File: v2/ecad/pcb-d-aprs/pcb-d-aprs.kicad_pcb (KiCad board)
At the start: 4 copper layers, 80 x 62 mm, 95 parts, among them Q1 BC847 (PTT2, spare), Q2 BC847 (PTT to the module), Q3 2N7002 (EMCON inhibit in Q2 e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, Q4 BC857 (TR mirror from RADIO_P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, U1 TPS61089 boost 7.6 V / 2 A, U2 DNP bench: DMR858M 5 W UHF mo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, U5 WM8960 audio codec QFN-32 (pi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, U7 PCA9555PW 0x26: PTT, PTT2, LE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, U8 SC16IS740IPW I2C-to-UART brid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, X1 24 MHz 3.3 V oscillator 3225 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

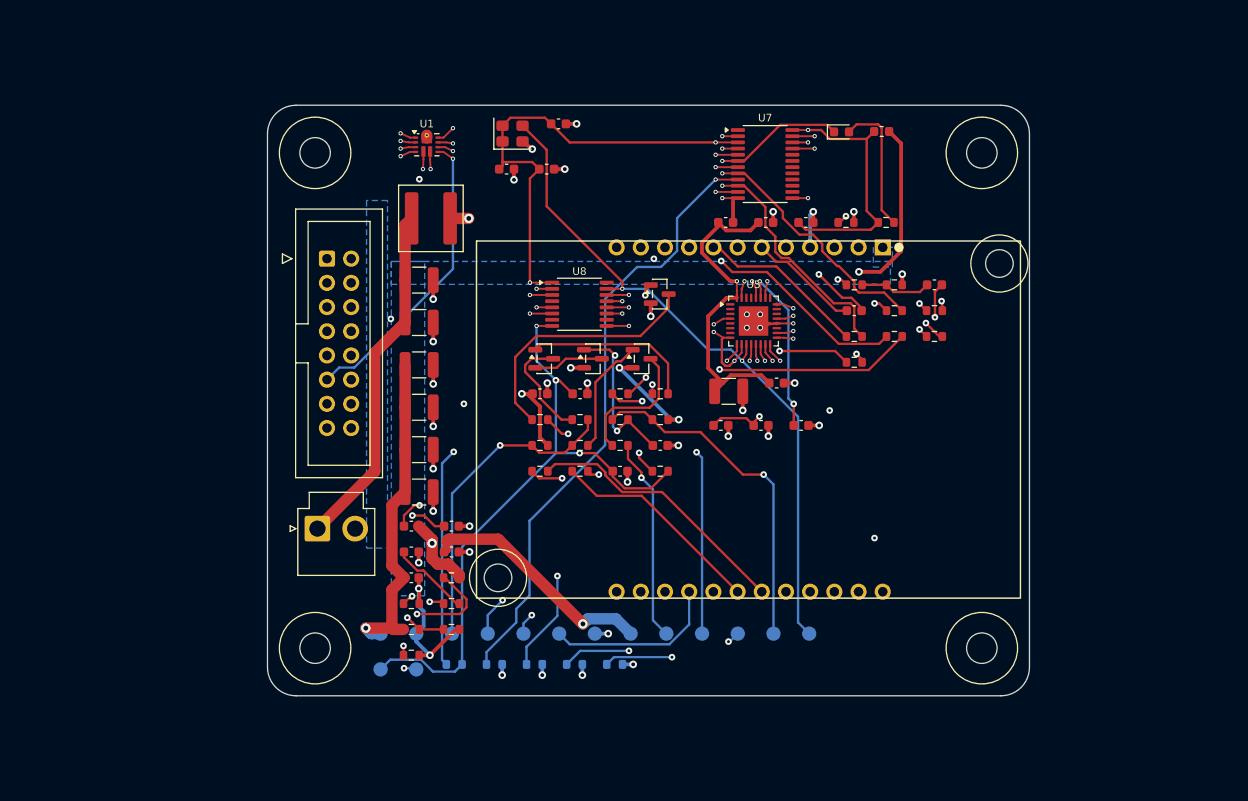
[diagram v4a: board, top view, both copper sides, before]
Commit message: feat(pcb-d): D7 routed and finished for the DMR858M V1.0 board [MESHSAT-804]
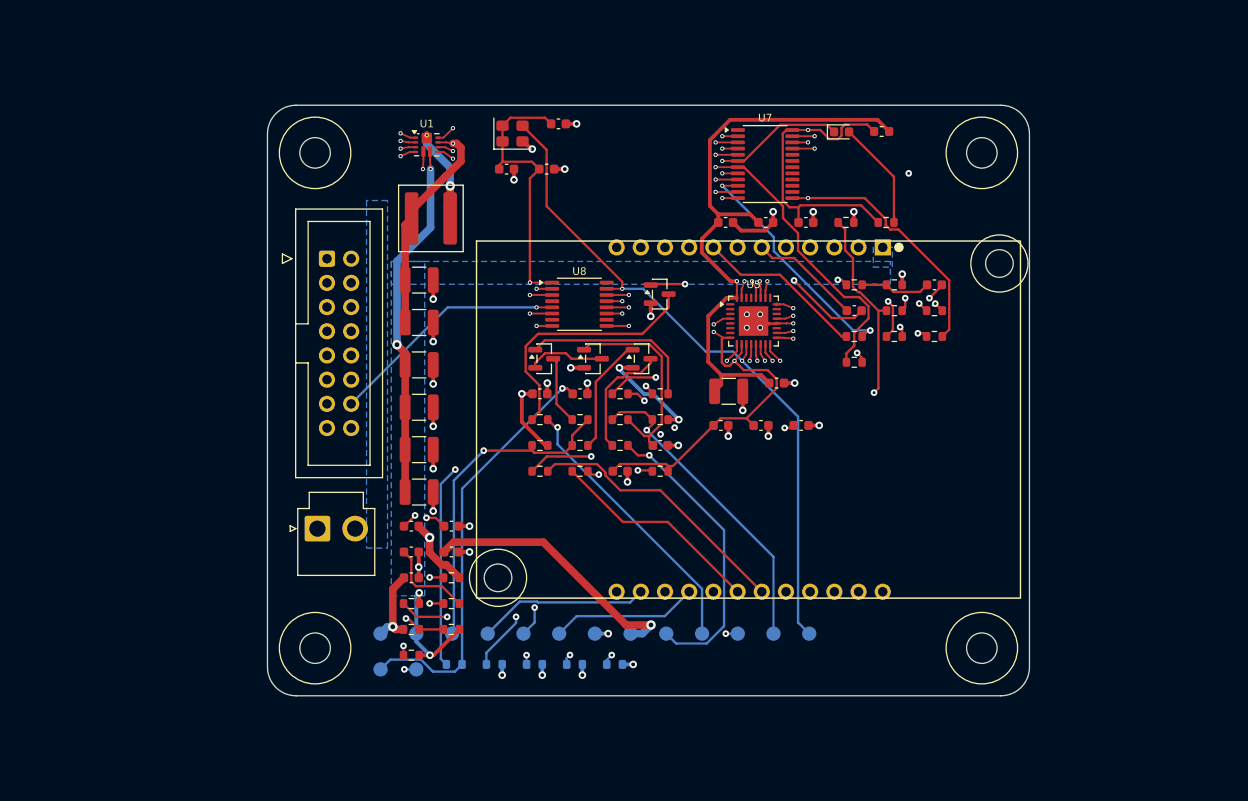
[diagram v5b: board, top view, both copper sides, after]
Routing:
- net /V8: track 36.9 -> 126.7 mm, vias 2 -> 3
- net GND: track 382.2 -> 454.6 mm
- net /VIN_CELL: track 95.6 -> 147.3 mm
- net /MEZZ_EN: track 99.3 -> 131.8 mm
- net /CH2_IN: track 84.9 -> 106.6 mm
- net /RADIO_SPK: track 80.2 -> 63.2 mm
- net /TX_INHIBIT_n: track 83.9 -> 69.1 mm
- net /SW: track 69.5 -> 55.3 mm
- net /RADIO_COS: track 77.9 -> 65.2 mm, vias 3 -> 1
- net /FSW: track 63.6 -> 51.3 mm
- net /+3V3_AB: track 230.1 -> 241.5 mm, vias 12 -> 10
- net /TR_APRS: track 67.6 -> 77.7 mm
- net /SDA: track 82.1 -> 92.1 mm, vias 4 -> 3
- net /RADIO_PTT: track 91.3 -> 81.4 mm, vias 1 -> 2
- net /RADIO_COS_IN: track 26.1 -> 35.9 mm, vias 1 -> 3
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
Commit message: fix(pcb): A21 and D7 boards retitled to their phase and date, deliverables re-exported [MESHSAT-795]
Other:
- board text added: "PCB-D APRS BOARD REV A (D7) | MESHSAT-709/748/804 | 2026-09-05"
- board text removed: "PCB-D APRS BOARD REV A (D5) | MESHSAT-709/748 | 2026-09-03"
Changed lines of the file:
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@@
 	(title_block
 		(title "MeshSat Field Kit carrier - PCB-D APRS BOARD")
-		(date "2026-09-02")
-		(rev "A")
+		(date "2026-09-05")
+		(rev "A (D7)")
 		(company "MeshSat")
 		(comment 1 "MESHSAT-709 / MESHSAT-748. Board-local frame, +X = case east. Phase D1 mechanical + placement. tools/gen_pcb_d.py")
@@
 		)
 	)
-	(gr_text "PCB-D APRS BOARD REV A (D5) | MESHSAT-709/748 | 2026-09-03"
+	(gr_text "PCB-D APRS BOARD REV A (D7) | MESHSAT-709/748/804 | 2026-09-05"
 		(at 110 101.5 0)
 		(layer "B.SilkS")

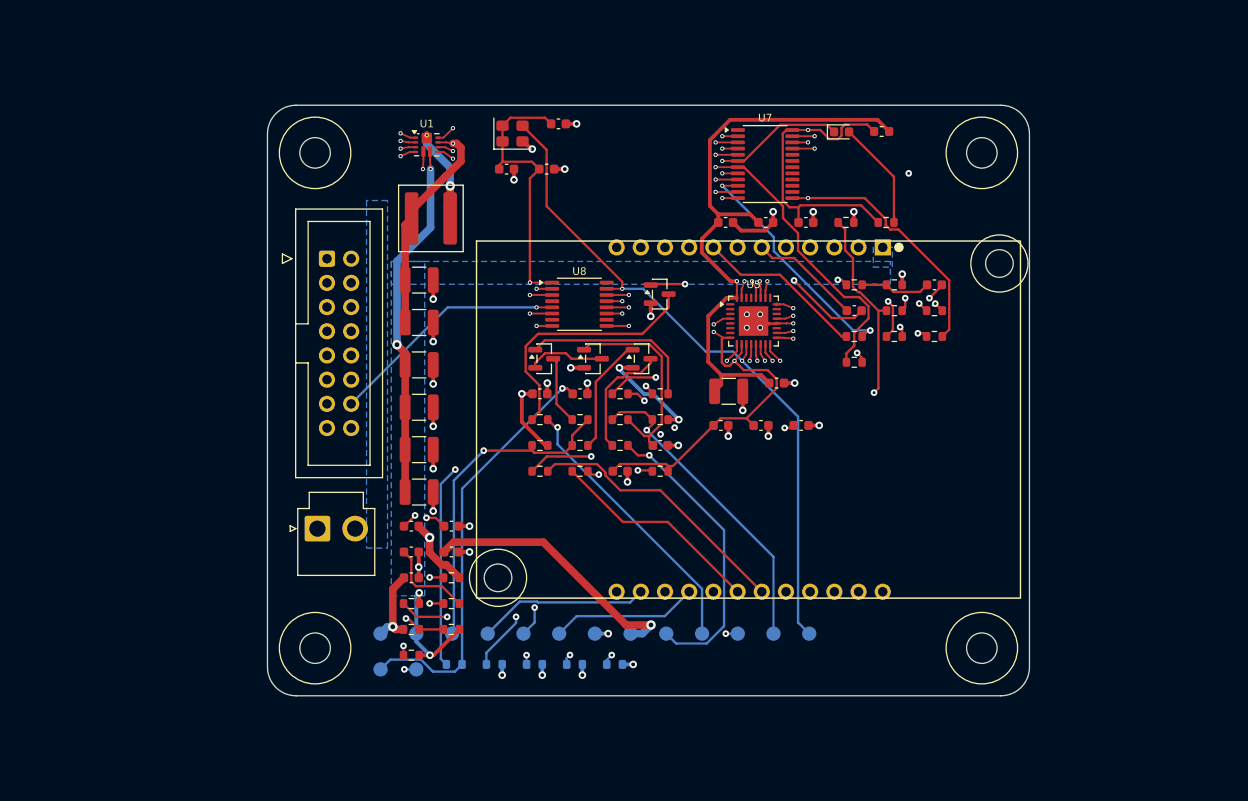
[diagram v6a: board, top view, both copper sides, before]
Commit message: feat(ecad): D8 routed clean and released (SA868 exciter, T/R relay, LPF, USB audio and control set), C7 generators (backer ring, RP2040 panel controller, PDi e-paper driver, Xenarc face, headset jacks), per-closure stub acceptance, plane-net fanout fixes [MESHSAT-830]
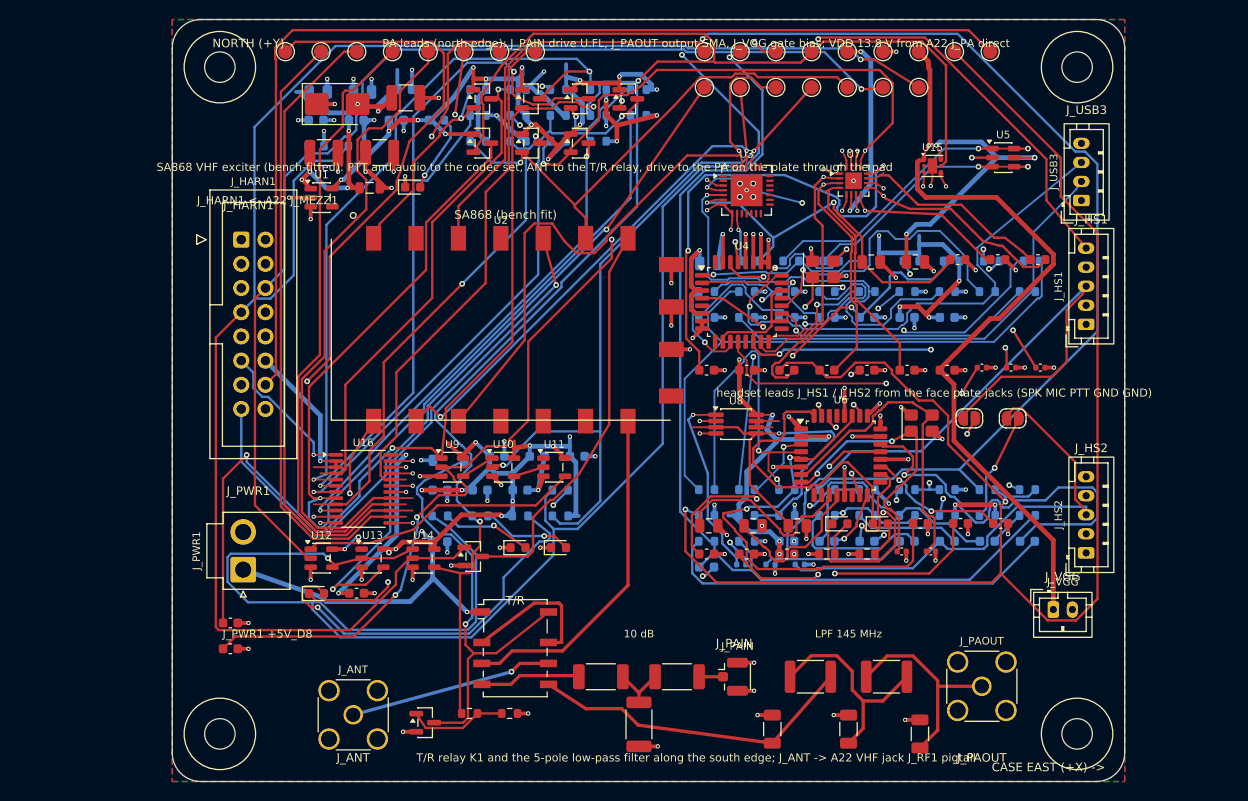
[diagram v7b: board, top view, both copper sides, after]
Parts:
- removed X1: 24 MHz 3.3 V oscillator 3225 (ASE-24.000MHZ-LC-T class), Oscillator_SMD_Abracon_ASE-4Pin_3.2x2.5mm
- added C1: 47u 6.3V X5R 1210, C_1210_3225Metric, F.Cu at (74.5, 68.2)
- added C11: 100n, C_0603_1608Metric, F.Cu at (132.5, 85.2)
- added C12: 1u, C_0603_1608Metric, B.Cu at (122.9, 91.3)
- added C15: 100n, C_0603_1608Metric, B.Cu at (127.2, 91.3)
- added C16: 100n, C_0603_1608Metric, B.Cu at (131.4, 91.3)
- added C19: 1u, C_0603_1608Metric, F.Cu at (128.6, 112.9)
- added C2: 47u 6.3V X5R 1210, C_1210_3225Metric, F.Cu at (65.9, 74.0)
- added C3: 10u, C_0805_2012Metric, B.Cu at (65.3, 67.6)
- added C31: 1u, C_0603_1608Metric, F.Cu at (106.1, 96.8)
- added C4: 100n, C_0603_1608Metric, B.Cu at (74.4, 67.4)
- added C41: 1u, C_0603_1608Metric, B.Cu at (127.2, 114.8)
- added C42: 1u, C_0603_1608Metric, B.Cu at (131.4, 114.8)
- added C43: 100p NP0, C_0402_1005Metric, B.Cu at (109.7, 117.2)
- added C44: 1n NP0, C_0402_1005Metric, B.Cu at (112.8, 117.2)
- added C45: 1n NP0, C_0402_1005Metric, B.Cu at (115.9, 117.2)
- added C46: 1u, C_0603_1608Metric, B.Cu at (135.6, 114.8)
- added C47: 1u, C_0603_1608Metric, B.Cu at (139.8, 114.8)
- added C48: 1u, C_0603_1608Metric, B.Cu at (106.1, 117.5)
- added C49: 100n, C_0603_1608Metric, F.Cu at (56.1, 123.4)
- added C5: 47u 6.3V X5R 1210, C_1210_3225Metric, F.Cu at (71.8, 74.0)
- added C50: 100n, C_0603_1608Metric, F.Cu at (56.1, 126.1)
- added C51: 100n, C_0603_1608Metric, B.Cu at (84.1, 105.9)
- added C52: 100n, C_0603_1608Metric, B.Cu at (88.3, 105.9)
- added C53: 100n, C_0603_1608Metric, B.Cu at (92.5, 105.9)
- added C54: 100n, C_0603_1608Metric, B.Cu at (78.1, 109.4)
- added C55: 100n, C_0603_1608Metric, B.Cu at (82.3, 109.4)
- added C56: 100n, C_0603_1608Metric, B.Cu at (86.5, 109.4)
- added C57: 100n, C_0603_1608Metric, B.Cu at (78.1, 114.8)
- added C58: 22p 500V NP0 1206, C_1206_3216Metric, F.Cu at (128.5, 135.0)
- added C59: 39p 500V NP0 1206, C_1206_3216Metric, F.Cu at (121.0, 134.5)
- added C6: 100n, C_0603_1608Metric, B.Cu at (65.1, 70.6)
- added C60: 22p 500V NP0 1206, C_1206_3216Metric, F.Cu at (113.0, 134.5)
- added C61: 4.7n, C_0402_1005Metric, F.Cu at (141.1, 96.5)
- added C62: 100n, C_0603_1608Metric, F.Cu at (131.4, 96.8)
- added C63: 100n, C_0603_1608Metric, F.Cu at (69.4, 120.2)
- added D2: 1N4148W coil flyback, D_SOD-123, B.Cu at (79.0, 106.3)
- added JP1: electret bias headset 1 (close for an electret microphone), SolderJumper-2_P1.3mm_Open_RoundedPad1.0x1.5mm, F.Cu at (133.7, 101.9)
- added JP2: electret bias headset 2, SolderJumper-2_P1.3mm_Open_RoundedPad1.0x1.5mm, F.Cu at (138.2, 101.9)
- added J_ANT: antenna (SMA, pigtail to A22's VHF jack J_RF1), SMA_Amphenol_132134_Vertical, F.Cu at (69.0, 133.0)
- added J_HS1: headset 1 lead (JST-PH 1x5 to the face plate U-174/U jack):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, JST_PH_B5B-PH-K_1x05_P2.00mm_Vertical, F.Cu at (145.9, 92.0)
- added J_HS2: headset 2 lead (JST-PH 1x5 to the face plate U-174/U jack):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, JST_PH_B5B-PH-K_1x05_P2.00mm_Vertical, F.Cu at (145.9, 116.0)
- added J_PAIN: PA drive (U.FL, coax to the RA30H1317M1 input on the plate), U.FL_Hirose_U.FL-R-SMT-1_Vertical, F.Cu at (108.9, 129.0)
- added J_PAOUT: PA output (SMA, coax from the RA30H1317M1 output on the pla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, SMA_Amphenol_132134_Vertical, F.Cu at (135.0, 130.0)
- added J_USB3: spare hub port 3 (JST-PH 1x4): 5V D- D+ GND, JST_PH_B4B-PH-K_1x04_P2.00mm_Vertical, F.Cu at (145.4, 79.0)
- added J_VGG: PA gate bias lead (JST-PH 1x2 to the RA30H1317M1 VGG): VGG 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, JST_PH_B2B-PH-K_1x02_P2.00mm_Vertical, F.Cu at (142.5, 122.0)
- added K1: Omron G6K-2F-Y 5 VDC DPDT signal relay, T/R, Relay_DPDT_Omron_G6K-2F-Y, F.Cu at (86.0, 126.0)
- added L2: 68nH 1812 (LPF), L_1812_4532Metric, F.Cu at (117.0, 129.0)
- added LED1: green power, LED_0603_1608Metric, F.Cu at (75.2, 77.6)
- added LED2: amber record, LED_0603_1608Metric, F.Cu at (120.1, 112.9)
- added LED3: green playback, LED_0603_1608Metric, F.Cu at (124.3, 112.9)
- added LED4: red transmit, LED_0603_1608Metric, F.Cu at (86.3, 115.4)
- added LED5: amber PA keyed, LED_0603_1608Metric, F.Cu at (90.6, 115.4)
- added LED6: green receive (AUDIO_ON low), LED_0603_1608Metric, F.Cu at (65.1, 120.3)
- added Q5: 2N7002, SOT-23, F.Cu at (92.8, 68.3)
- added Q6: 2N7002, SOT-23, F.Cu at (97.9, 68.3)
- added Q7: 2N7002, SOT-23, F.Cu at (82.6, 73.0)
- added Q8: 2N7002, SOT-23, F.Cu at (87.7, 73.0)
- added Q9: 2N7002, SOT-23, F.Cu at (92.8, 73.0)
- added R1: 2.2k, R_0603_1608Metric, B.Cu at (77.7, 70.6)
- added R14: 15k, R_0603_1608Metric, B.Cu at (110.3, 88.6)
- added R16: 22, R_0603_1608Metric, B.Cu at (118.7, 88.6)
- added R17: 22, R_0603_1608Metric, B.Cu at (122.9, 88.6)
- added R18: 15k, R_0603_1608Metric, B.Cu at (127.2, 88.6)
- added R19: 15k, R_0603_1608Metric, B.Cu at (131.4, 88.6)
- added R20: 22, R_0603_1608Metric, B.Cu at (135.6, 88.6)
- added R21: 22, R_0603_1608Metric, B.Cu at (139.8, 88.6)
- added R22: 15k, R_0603_1608Metric, B.Cu at (106.1, 91.3)
- added R23: 15k, R_0603_1608Metric, B.Cu at (110.3, 91.3)
- added R24: 15k, R_0603_1608Metric, B.Cu at (114.5, 91.3)
- added R25: 15k, R_0603_1608Metric, B.Cu at (118.7, 91.3)
- added R26: 33, R_0603_1608Metric, B.Cu at (106.1, 109.4)
- added R27: 33, R_0603_1608Metric, B.Cu at (110.3, 109.4)
- added R28: 1.5k, R_0603_1608Metric, B.Cu at (114.5, 109.4)
- added R29: 1k, R_0603_1608Metric, F.Cu at (118.7, 116.1)
- added R5: 10k, R_0603_1608Metric, B.Cu at (90.7, 112.1)
- added R53: 100k, R_0603_1608Metric, F.Cu at (85.4, 132.9)
- added R54: 27 1% 2010, R_2010_5025Metric, F.Cu at (95.0, 129.0)
- added R55: 36 1% 2010, R_2010_5025Metric, F.Cu at (99.0, 134.0)
- added R56: 27 1% 2010, R_2010_5025Metric, F.Cu at (103.0, 129.0)
- added R6: 22, R_0603_1608Metric, B.Cu at (115.0, 85.4)
- added R66: 10k, R_0603_1608Metric, B.Cu at (82.1, 67.4)
- added R67: 10k, R_0603_1608Metric, B.Cu at (86.3, 67.4)
- added R68: 10k, R_0603_1608Metric, B.Cu at (90.5, 67.4)
- added R69: 10k, R_0603_1608Metric, B.Cu at (94.7, 67.4)
- added R7: 22, R_0603_1608Metric, B.Cu at (119.2, 85.4)
- added R70: 10k, R_0603_1608Metric, B.Cu at (98.9, 67.4)
- added R71: 10k, R_0603_1608Metric, B.Cu at (82.1, 70.1)
- added R72: 10k, R_0603_1608Metric, B.Cu at (86.3, 70.1)
- added R73: 10k, R_0603_1608Metric, B.Cu at (90.5, 70.1)
- added R74: 10k, R_0603_1608Metric, B.Cu at (94.7, 70.1)
- added R75: 10k, R_0603_1608Metric, B.Cu at (98.9, 70.1)
- added R76: 10k, R_0603_1608Metric, B.Cu at (82.1, 72.8)
- added R77: 10k, R_0603_1608Metric, B.Cu at (86.3, 72.8)
- added R78: 10k, R_0603_1608Metric, B.Cu at (90.5, 72.8)
- added R79: 10k, R_0603_1608Metric, B.Cu at (94.7, 72.8)
- added TP16: PA_EN, TestPoint_Pad_D1.5mm, F.Cu at (128.4, 67.1)
- added TP17: EXP_SPARE1, TestPoint_Pad_D1.5mm, F.Cu at (61.9, 63.4)
- added TP18: EXP_SPARE2, TestPoint_Pad_D1.5mm, F.Cu at (65.6, 63.4)
- added TP19: EXP_SPARE3, TestPoint_Pad_D1.5mm, F.Cu at (69.4, 63.4)
- added TP20: EXP_SPARE4, TestPoint_Pad_D1.5mm, F.Cu at (73.1, 63.4)
- added TP21: EXP_SPARE5, TestPoint_Pad_D1.5mm, F.Cu at (76.9, 63.4)
- added TP22: EXP_SPARE6, TestPoint_Pad_D1.5mm, F.Cu at (80.6, 63.4)
- added TP23: EXP_SPARE7, TestPoint_Pad_D1.5mm, F.Cu at (84.4, 63.4)
- added TP24: EXP_SPARE8, TestPoint_Pad_D1.5mm, F.Cu at (88.1, 63.4)
- added U10: 74LVC1G08 AND: headsets AND software PTT (RTS), SOT-23-5, F.Cu at (84.8, 107.0)
- added U11: 74LVC1G04 inverter (2 A 4 Y): PTT_ANY, SOT-23-5, F.Cu at (90.1, 107.0)
- added U12: 74LVC1G08 AND: KEY = PTT_ANY AND TX_INHIBIT_n (the panel's 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, SOT-23-5, F.Cu at (65.7, 116.5)
- added U13: 74LVC1G04 inverter: KEY -> SA868 PTT (low = transmit), SOT-23-5, F.Cu at (71.0, 116.5)
- added U14: 74LVC1G08 AND: PA_KEY = KEY AND PA_EN (A22's PA rail state), SOT-23-5, F.Cu at (76.4, 116.5)
- added U15: TPS22810DRV, WSON-6-1EP_2x2mm_P0.65mm_EP1x1.6mm, F.Cu at (129.8, 75.4)
- added U16: PCA9555PW 0x26: COS, PTT states, KEY, PA_KEY in; exciter PD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, TSSOP-24_4.4x7.8mm_P0.65mm, F.Cu at (70.0, 109.3)
- added U3: CP2102N-A02-GQFN28 USB-UART bridge (SAU), QFN-28-1EP_5x5mm_P0.5mm_EP3.35x3.35mm, F.Cu at (110.3, 77.9)
- added U4: TUSB2046BI four-port USB 2.0 full-speed hub (LQFP-32; BUSPW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, LQFP-32_7x7mm_P0.8mm, F.Cu at (109.8, 89.7)
- added U6: TI PCM2912A USB audio codec (TQFP-32): mono input from the 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, TQFP-32_7x7mm_P0.8mm, F.Cu at (120.2, 105.8)
- added U9: 74LVC1G08 AND (1 A 2 B 3 GND 4 Y 5 VCC): both headset PTT l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, SOT-23-5, F.Cu at (79.4, 107.0)
- added Y1: 6 MHz 3225 (CL 20 pF; C1 = C2 = 27 pF and Rd 1.5k per SLLS4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, Crystal_SMD_3225-4Pin_3.2x2.5mm, F.Cu at (118.3, 86.2)
- added Y2: 6 MHz 3225 (codec clock; 18 pF loads, to confirm on the EVM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, Crystal_SMD_3225-4Pin_3.2x2.5mm, F.Cu at (128.7, 102.4)
- C10: footprint C_0603_1608Metric -> C_0805_2012Metric
- C13, C14: value 4.7u -> 27p NP0; footprint C_0603_1608Metric -> C_0402_1005Metric
- C17, C9: value 100n -> 10u; footprint C_0603_1608Metric -> C_0805_2012Metric; moved to B.Cu
- C18, C8: value 100n -> 1u; moved to B.Cu
- C20, C30: value 100n 25V -> 1u
- C22: value 4.7n -> 1u
- C23: value 22u 10V X7R 1210 -> 1u; footprint C_1210_3225Metric -> C_0603_1608Metric
- C24: value 22u 10V X7R 1210 -> 10u; footprint C_1210_3225Metric -> C_0805_2012Metric
- C25, C33, C40: value 100n -> 10u; footprint C_0603_1608Metric -> C_0805_2012Metric
- C26, C27: value 22u 25V X7R 1210 -> 18p NP0; footprint C_1210_3225Metric -> C_0402_1005Metric
- C28: value 22u 25V X7R 1210 -> 1u; footprint C_1210_3225Metric -> C_0603_1608Metric; moved to B.Cu
- C29: value 22u 25V X7R 1210 -> 1u; footprint C_1210_3225Metric -> C_0603_1608Metric
- C32, C35, C36, C38: value 100n -> 1u
- C34: value 10u -> 1u; footprint C_1210_3225Metric -> C_0603_1608Metric; moved to B.Cu
- C37: value 4.7u -> 1u
- C7: value 4.7u -> 1u; moved to B.Cu
- D1: value green status (U7 bit 3 sinks) -> SMBJ5.0A; footprint LED_0603_1608Metric -> D_SMB
- FB1: value 600R@100MHz -> 600R 2A ferrite (the exciter's 1 A transmit pulses); footprint L_0603_1608Metric -> L_0805_2012Metric
- H1, H2, H3, H4: value M3 standoff to PCB-A -> M3 standoff on A22 (5/95, +-35)
- J_HARN1: value harness to PCB-A J_MEZZ1 (IDC 2x8): I2S, I2C, the gated 3.3 V from B13, PTT lines -> A22 mezzanine harness J_MEZZ1 (IDC 2x8): USB pair, PTT mirror, inhibit, PA rail state, I2C, 3.3 V
- J_PWR1: value cell node from PCB-A J_MEZZ_PWR (JST-VH) -> 5 V from A22 J_MEZZ_PWR1 (JST-VH, 2 A eFuse on A22): + -
- L1: value 1.5uH XAL6030-152MEB (Isat 12 A, 5.6 mOhm) -> 68nH 1812 (LPF, 145 MHz 5th order; values to be verified in MESHSAT-818); footprint L_Coilcraft_XAL6030-XXX -> L_1812_4532Metric
- Q1: value BC847 (PTT2, spare) -> 2N7002 PA_EN -> H/L low (never tie H/L high)
- Q2: value BC847 (PTT to the module) -> 2N7002 relay coil
- Q3: value 2N7002 (EMCON inhibit in Q2 emitter) -> 2N7002
- Q4: value BC857 (TR mirror from RADIO_PTT) -> 2N7002
- R10: value 1.5k -> 10k; moved to B.Cu
- R11, R3, R4, R47: moved to B.Cu
- R12, R13: value 22R -> 22; moved to B.Cu
- R15: value 1k -> 15k; moved to B.Cu
- R2: value 47k -> 100k; moved to B.Cu
- R30: value 301k 1% (500 kHz) -> 1k
- R31: value 100k 1% (ILIM 10 A peak, 9 A min) -> 10k; moved to B.Cu
- R32: value 17.4k -> 10k; moved to B.Cu
- R33: value 105k 1% -> 4.7k; moved to B.Cu
- R34: value 20k 1% -> 100k; moved to B.Cu
- R35, R38, R39: value 100k -> 10k; moved to B.Cu
- R37, R45, R46: value 1k -> 10k; moved to B.Cu
- R40: value 10k -> 4.7k; moved to B.Cu
- R41: value 100R -> 4.7k; moved to B.Cu
- R42: value 1k -> 220k; moved to B.Cu
- R43, R44: value 1k -> 2.2k; moved to B.Cu
- R48: value 1k -> 100; moved to B.Cu
- R49, R50: value 100k -> 1k
- R51: value 100k -> 2.2k
- R52: value 100k -> 1k; moved to F.Cu
- R8: value 100R -> 1.5k; moved to B.Cu
- R9: value 100R -> 10k; moved to B.Cu
- TP1: value V8 -> AF_OUT; moved to F.Cu
- TP10: value RADIO_PTT2 -> AB_SPARE; moved to F.Cu
- TP11: value MEZZ_EN -> SA_TXD; moved to F.Cu
- TP12: value TX_INHIBIT_n -> SA_RXD; moved to F.Cu
- TP13: value MCLK -> PTT_SW_n; moved to F.Cu
- TP14: value +3V3_AB -> SA_PD; moved to F.Cu
- TP15: value I2S_BCLK -> TX_INHIBIT_n; moved to F.Cu
- TP2: value GND -> MIC_SUM; moved to F.Cu
- TP3: value RADIO_PTT -> KEY; moved to F.Cu
- TP4: value RADIO_MIC -> PA_KEY; moved to F.Cu
- TP5: value RADIO_SPK -> +3V3_D8; moved to F.Cu
- TP6: value RADIO_COS -> +5V_D8; moved to F.Cu
- TP7: value +3V3 -> VGG_SW; moved to F.Cu
- TP8: value VIN_CELL -> RX_MIX; moved to F.Cu
- TP9: value TR_APRS -> ZEROIZE_HW; moved to F.Cu
- U1: value TPS61089 boost 7.6 V / 2 A -> TLV75533PDBV 3.3 V 500 mA LDO (1 IN 2 GND 3 EN 4 NC 5 OUT); footprint Texas_VQFN-RNR0011A-11 -> SOT-23-5
- U2: value DNP bench: DMR858M 5 W UHF module on 2 x 1x12 2.54 mm female headers 8.5 mm + M2.5 x 11 mm standoffs -> NiceRF SA868 VHF 2 W exciter, bench-fitted (castellated; VBAT 3.3 to 5.5 V, TX 1 A); footprint DMR858M -> NiceRF_SA868
- U5: value WM8960 audio codec QFN-32 (pins per datasheet table: 4 LINPUT1, 11 MCLK, 12 BCLK, 13 DACLRC, 14 DACDAT, 15 ADCLRC, 16 A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 -> USBLC6-2SC6; footprint QFN-32-1EP_5x5mm_P0.5mm_EP3.1x3.1mm -> SOT-23-6
- U7: value PCA9555PW 0x26: PTT, PTT2, LED, CS, COS in, channel code in -> TI TPA6132A2 headphone amplifier (QFN-16), receive audio to the two headset leads; footprint TSSOP-24_4.4x7.8mm_P0.65mm -> QFN-16-1EP_3x3mm_P0.5mm_EP1.75x1.75mm
- U8: value SC16IS740IPW I2C-to-UART bridge 0x48, 24 MHz external clock on XTAL1 -> TLV9062IDGK dual op amp (1 OUT1 2 IN1- 3 IN1+ 4 V- 5 IN2+ 6 IN2- 7 OUT2 8 V+): A the mic sum, B unused as a follower; footprint TSSOP-16_4.4x5mm_P0.65mm -> VSSOP-8_3x3mm_P0.65mm
- moved TP14 78.3 mm to (120.9, 67.1)
- moved TP15 78.3 mm to (124.6, 67.1)
- moved C30 73.8 mm to (140.9, 85.2)
- moved TP1 69.9 mm to (105.9, 63.4)
- moved TP2 69.9 mm to (109.6, 63.4)
- moved TP3 69.9 mm to (113.4, 63.4)
- moved TP4 69.9 mm to (117.1, 63.4)
- moved TP5 69.9 mm to (120.9, 63.4)
- moved TP6 69.9 mm to (124.6, 63.4)
- moved TP7 69.9 mm to (128.4, 63.4)
- moved TP8 69.9 mm to (132.1, 63.4)
- moved TP9 69.9 mm to (135.9, 63.4)
- moved L1 67.9 mm to (125.0, 129.0)
- moved C29 65.5 mm to (136.7, 85.2)
- moved R35 62.9 mm to (135.6, 109.4)
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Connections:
- C10 pad 1: /+3.3VA -> /SAU_3V3
- C13 pad 1: /MIC_NODE -> /HUB_XTAL1
- C13 pad 2: /RADIO_MIC -> GND
- C14 pad 1: /RADIO_SPK -> /HUB_XTAL2R
- C14 pad 2: /SPK_IN -> GND
- C17 pad 1: +3V3 -> /+3V3_D8
- C18 pad 1: /+3V3_AB -> /+5V_D8
- C20 pad 1: /BOOT -> /PCM_VCCA
- C20 pad 2: /SW -> GND
- C21 pad 1: /BST_VCC -> /PCM_VCCL
- C22 pad 1: /COMPC -> /PCM_VCCR
- C23 pad 1: /VIN_CELL -> /PCM_VCCP
- C24 pad 1: /VIN_CELL -> /PCM_VCOM1
- C25 pad 1: /VIN_CELL -> /PCM_VCOM2
- C26 pad 1: /V8 -> /PCM_XTI
- C27 pad 1: /V8 -> /PCM_XTO
- C28 pad 1: /V8 -> /AF_DIV
- C28 pad 2: GND -> /PCM_VIN
- C29 pad 1: /V8 -> /AMP_HPVSS
- C30 pad 1: /V8 -> /AMP_CPP
- C30 pad 2: GND -> /AMP_CPN
- C32 pad 1: /Q3_G -> /+5V_D8
- C33 pad 1: /+3.3VA -> /+5V_D8
- C34 pad 1: /+3.3VA -> /PCM_VOUTL
- C34 pad 2: GND -> /PCM_L_AC
- C35 pad 1: /+3V3_AB -> /RX_MIX
- C35 pad 2: GND -> /AMP_INL_P
- C36 pad 1: /+3V3_AB -> /RX_MIX
- C36 pad 2: GND -> /AMP_INR_P
- C37 pad 1: /VMID -> /AMP_INL_N
- C38 pad 1: /+3V3_AB -> /AMP_INR_N
- C39 pad 1: /+3V3_AB -> /+5V_D8
- C40 pad 1: /+3V3_AB -> /VREF
- C7 pad 1: /+3V3_AB -> /+5V_D8
- C8 pad 1: /+3V3_AB -> /+3V3_D8
- C9 pad 1: /+3.3VA -> /+3V3_D8
- D1 pad 1: /LED_K -> GND
- D1 pad 2: /LED_A -> /+5V_D8
- FB1 pad 1: /+3V3_AB -> /+5V_D8
- FB1 pad 2: /+3.3VA -> /+5V_SA
- J_HARN1 pad 10: /TR_APRS -> /SCL
- J_HARN1 pad 11: /MEZZ_EN -> /EXP_INT
- J_HARN1 pad 12: +3V3 -> /+3V3
- J_HARN1 pad 14: /SCL -> /ZEROIZE_HW
- J_HARN1 pad 15: /TX_INHIBIT_n -> /AB_SPARE
- J_HARN1 pad 2: /+3V3_AB -> /USB_D8_P
- J_HARN1 pad 3: /I2S_BCLK -> /USB_D8_N
- J_HARN1 pad 4: /I2S_LRCLK -> GND
- J_HARN1 pad 5: GND -> /TR_APRS
- J_HARN1 pad 6: /I2S_DOUT -> /TX_INHIBIT_n
- J_HARN1 pad 7: /I2S_DIN -> /PA_EN
- J_PWR1 pad 1: /VIN_CELL -> /+5V_D8
- L1 pad 1: /VIN_CELL -> /RF_PAOUT
- L1 pad 2: /SW -> /RF_LPF_M
- Q1 pad 1: /Q1_B -> /PA_EN
- Q1 pad 3: /Q1_C -> /SA_HL
- Q2 pad 1: /Q2_B -> /RLY_DRV
- Q2 pad 2: /Q2_E -> GND
- Q2 pad 3: /Q2_C -> /RLY_K
- Q3 pad 1: /Q3_G -> /+3V3_D8
- Q3 pad 2: GND -> /SA_AUDIO_ON_n
- Q3 pad 3: /Q2_E -> /X_COS_n
- Q4 pad 1: /Q4_B -> /+3V3_D8
- Q4 pad 2: +3V3 -> /PTT_HS1_n
- Q4 pad 3: /Q4_C -> /X_PTT_HS1_n
- R10 pad 1: /OUT2 -> /HUB_RST_n
- R10 pad 2: /Q1_B -> /+3V3_D8
- R11 pad 1: /OUT1 -> /HUB_XTAL2R
- R11 pad 2: /Q2_B -> /HUB_XTAL2
- R12 pad 1: /Q1_C -> /HUB_DP1
- R12 pad 2: /RADIO_PTT2 -> /USB1_P
- R13 pad 1: /Q2_C -> /HUB_DM1
- R13 pad 2: /RADIO_PTT -> /USB1_N
- R15 pad 1: /+3V3_AB -> /USB1_N
- R15 pad 2: /LED_A -> GND
- R2 pad 1: /AFOUT -> /TX_INHIBIT_n
- R2 pad 2: /MIC_NODE -> GND
- R3 pad 1: /RADIO_COS -> /PA_EN
- R30 pad 1: /FSW -> /+3V3_D8
- R30 pad 2: /SW -> /LED_PLAY_A
- R31 pad 1: /ILIM -> /AF_OUT
- R31 pad 2: GND -> /AF_DIV
- R32 pad 1: /COMP -> /AF_DIV
- R32 pad 2: /COMPC -> GND
- R33 pad 1: /V8 -> /X_MMUTE
- R33 pad 2: /FB8 -> /MMUTE
- R34 pad 1: /FB8 -> /MMUTE
- R35 pad 1: /MEZZ_EN -> /AF_OUT
- R35 pad 2: GND -> /RX_MIX
- R36 pad 1: /CS -> /PCM_L_AC
- R36 pad 2: /+3V3_AB -> /RX_MIX
- R37 pad 1: /TX_INHIBIT_n -> /RX_MIX
- R37 pad 2: /Q3_G -> GND
- R38 pad 1: /TX_INHIBIT_n -> /+5V_D8
- R38 pad 2: +3V3 -> /VREF
- R39 pad 1: /RADIO_PTT -> /VREF
- R39 pad 2: +3V3 -> GND
- R4 pad 1: /MIC_NODE -> /SAU_RST
- R4 pad 2: GND -> /SAU_3V3
- R40 pad 1: /RADIO_PTT -> /HS1_MIC_AC
- R40 pad 2: /Q4_B -> /MICAMP_IN_N
- R41 pad 1: /Q4_C -> /HS2_MIC_AC
- R41 pad 2: /TR_APRS -> /MICAMP_IN_N
- R42 pad 1: /RADIO_COS -> /MICAMP_OUT
- R42 pad 2: /RADIO_COS_IN -> /MICAMP_IN_N
- R43 pad 1: /CH8 -> /HS1_BIAS_R
- R43 pad 2: /CH8_IN -> /+5V_D8
- R44 pad 1: /CH4 -> /HS2_BIAS_R
- R44 pad 2: /CH4_IN -> /+5V_D8
- R45 pad 1: /CH2 -> /MICAMP_AC
- R45 pad 2: /CH2_IN -> /MIC_SUM
- R46 pad 1: /CH1 -> /PCM_R_AC
- R46 pad 2: /CH1_IN -> /MIC_SUM
- R47 pad 1: /BR_nRST -> /MIC_SUM
- R47 pad 2: /+3V3_AB -> GND
- R48 pad 1: /CS_CTL -> /KEY
- R48 pad 2: /CS -> /TR_APRS
- R49 pad 1: /CH8_IN -> /KEY
- R49 pad 2: GND -> /LED_TX_A
- R50 pad 1: /CH4_IN -> /PA_KEY
- R50 pad 2: GND -> /LED_PA_A
- R51 pad 1: /CH2_IN -> /+3V3_D8
- R51 pad 2: GND -> /LED_RX_A
- R52 pad 1: /CH1_IN -> /PA_KEY
- R52 pad 2: GND -> /RLY_DRV
- R8 pad 1: /BR_TX -> /HUB_DP0
- R8 pad 2: /RADIO_RX -> /+3V3_D8
- R9 pad 1: /RADIO_TX -> /HUB_OVRCUR_n
- R9 pad 2: /BR_RX -> /+3V3_D8
- TP1 pad 1: /V8 -> /AF_OUT
- TP10 pad 1: /RADIO_PTT2 -> /AB_SPARE
- TP11 pad 1: /MEZZ_EN -> /SA_TXD
- TP12 pad 1: /TX_INHIBIT_n -> /SA_RXD
- TP13 pad 1: /MCLK -> /PTT_SW_n
- TP14 pad 1: /+3V3_AB -> /SA_PD
- TP15 pad 1: /I2S_BCLK -> /TX_INHIBIT_n
- TP2 pad 1: GND -> /MIC_SUM
- TP3 pad 1: /RADIO_PTT -> /KEY
- TP4 pad 1: /RADIO_MIC -> /PA_KEY
- TP5 pad 1: /RADIO_SPK -> /+3V3_D8
- TP6 pad 1: /RADIO_COS -> /+5V_D8
- TP7 pad 1: +3V3 -> /VGG_SW
- TP8 pad 1: /VIN_CELL -> /RX_MIX
- TP9 pad 1: /TR_APRS -> /ZEROIZE_HW
- U1 pad 1: /FSW -> /+5V_D8
- U1 pad 2: /BST_VCC -> GND
- U1 pad 3: /FB8 -> /+5V_D8
- U1 pad 4: /COMP -> (no net)
- U1 pad 5: GND -> /+3V3_D8
- U2 pad 1: /V8 -> /SA_AUDIO_ON_n
- U2 pad 10: /CH1 -> GND
- U2 pad 12: (no net) -> /RF_SA
- U2 pad 13: GND -> (no net)
- U2 pad 14: /RADIO_MIC -> (no net)
- U2 pad 15: GND -> (no net)
- U2 pad 16: /RADIO_COS -> /SA_RXD
- U2 pad 17: GND -> /SA_TXD
- U2 pad 18: /RADIO_TX -> /MIC_IN
- U2 pad 2: GND -> (no net)
- U2 pad 3: /CS -> /AF_OUT
- U2 pad 4: GND -> (no net)
- U2 pad 5: /RADIO_PTT -> /SA_PTT_n
- U2 pad 6: /RADIO_SPK -> /SA_PD
- U2 pad 7: /CH8 -> /SA_HL
- U2 pad 8: /CH4 -> /+5V_SA
- U2 pad 9: /CH2 -> GND
- U5 pad 1: (no net) -> /USB_D8_P
- U5 pad 2: (no net) -> GND
- U5 pad 3: (no net) -> /USB_D8_N
- U5 pad 4: /SPK_IN -> /USB_D8_N
- U5 pad 5: (no net) -> /+5V_D8
- U5 pad 6: (no net) -> /USB_D8_P
- U7 pad 1: (no net) -> /AMP_INL_N
- U7 pad 10: /CH4_IN -> GND
- U7 pad 11: /CH2_IN -> /AMP_CPP
- U7 pad 12: GND -> /AMP_HPVDD
- U7 pad 13: /CH1_IN -> /AMP_EN
- U7 pad 14: (no net) -> /+5V_D8
- U7 pad 15: (no net) -> GND
- U7 pad 16: (no net) -> /HS1_SPK
- U7 pad 17: (no net) -> GND
- U7 pad 2: /+3V3_AB -> /AMP_INL_P
- U7 pad 3: /+3V3_AB -> /AMP_INR_P
- U7 pad 4: /OUT1 -> /AMP_INR_N
- U7 pad 5: /OUT2 -> /HS2_SPK
- U7 pad 6: /LED_K -> /+3V3_D8
- U7 pad 7: /CS_CTL -> GND
- U7 pad 8: /RADIO_COS_IN -> /AMP_HPVSS
- U7 pad 9: /CH8_IN -> /AMP_CPN
- U8 pad 1: /+3V3_AB -> /MICAMP_OUT
- U8 pad 2: /+3V3_AB -> /MICAMP_IN_N
- U8 pad 3: /+3V3_AB -> /VREF
- U8 pad 4: (no net) -> GND
- U8 pad 5: /SCL -> /VREF
- U8 pad 6: /SDA -> /OPB_OUT
- U8 pad 7: (no net) -> /OPB_OUT
- U8 pad 8: /+3V3_AB -> /+5V_D8
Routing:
- net /+3V3_D8: track 0.00 -> 348.6 mm, vias 0 -> 38
- net /+5V_D8: track 0.00 -> 327.5 mm, vias 0 -> 24
- net GND: track 454.6 -> 174.2 mm, vias 47 -> 114
- net /+3V3_AB: track 241.5 -> 0.00 mm, vias 10 -> 0
- net /KEY: track 0.00 -> 203.3 mm, vias 0 -> 5
- net /PTT_HS2_n: track 0.00 -> 190.2 mm, vias 0 -> 4
- net /PA_EN: track 0.00 -> 181.8 mm, vias 0 -> 1
- net /PA_KEY: track 0.00 -> 172.9 mm, vias 0 -> 2
- net /PTT_HS1_n: track 0.00 -> 170.6 mm, vias 0 -> 5
- net /RX_MIX: track 0.00 -> 163.9 mm, vias 0 -> 2
- net /USB_D8_P: track 0.00 -> 149.8 mm, vias 0 -> 2
- net /VIN_CELL: track 147.3 -> 0.00 mm, vias 2 -> 0
- net /AF_OUT: track 0.00 -> 147.2 mm, vias 0 -> 1
- net /+3V3: track 0.00 -> 138.7 mm, vias 0 -> 8
- net /MEZZ_EN: track 131.8 -> 0.00 mm, vias 3 -> 0
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- added copper zone on B.Cu, net GND
- added copper zone on F.Cu, net GND
- added copper zone on In2.Cu, net GND
- removed copper zone on In2.Cu, net +3V3
- removed copper zone on B.Cu, net V8
- removed copper zone on B.Cu, net VIN_CELL
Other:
- board size 80 x 62 mm -> 100 x 80 mm
- board text added: "10 dB"
- board text added: "AUD"
- board text added: "BOARD DATUM = CASE (50, 0)"
- board text added: "CASE EAST (+X) ->"
- board text added: "CTRL"
- board text added: "HUB"
- board text added: "J_ANT"
- board text added: "J_HARN1"
- board text added: "J_HARN1 <- A22 J_MEZZ1"
- board text added: "J_HS1"
- board text added: "J_HS2"
- board text added: "J_PAIN"
- board text added: "J_PAOUT"
- board text added: "J_PWR1"
- board text added: "J_PWR1 +5V_D8"
- board text added: "J_USB3"
- board text added: "J_VGG"
- board text added: "LPF 145 MHz"
- board text added: "MESHSAT-830 | 100x80x1.6 4L | 2026-09-07"
- board text added: "NORTH (+Y)"
- board text added: "PA leads (north edge): J_PAIN drive U.FL, J_PAOUT output SMA, J_VGG gate bias; VDD 13.8 V from A22 J_PA direct"
- board text added: "PCB-D APRS MEZZANINE REV A (D8)"
- board text added: "RFP"
- board text added: "SA868 (bench fit)"
- board text added: "SA868 VHF exciter (bench-fitted): PTT and audio to the codec set, ANT to the T/R relay, drive to the PA on the plate through the pad"
- board text added: "T/R"
- board text added: "T/R relay K1 and the 5-pole low-pass filter along the south edge; J_ANT -> A22 VHF jack J_RF1 pigtail"
- board text added: "WEST"
- board text added: "headset leads J_HS1 / J_HS2 from the face plate jacks (SPK MIC PTT GND GND)"
- board text removed: "DMR858M on 2x 1x12 sockets + M2.5 x 11 standoffs, heatsink up"
- board text removed: "J_HARN1 to PCB-A J_MEZZ1"
- board text removed: "J_PWR1 MEZZ_CELL GND"
- board text removed: "N: D6 core (top clock/expander/LED, bottom codec/audio/PTT)"
- board text removed: "PCB-D APRS BOARD REV A (D7) | MESHSAT-709/748/804 | 2026-09-05"
- board text removed: "S: DNP headers (top), jumpers + TPs (bottom)"
- board text removed: "SMA"
- board text removed: "SMA east -> UHF bulkhead | USB-C west | pin 1 = VCC (NE)"
- board text removed: "W: 8 V boost"
- board text removed: "rows and holes per NiceRF datasheet V1.2 p.10"
- board text removed: "underside faces PCB-A: jumpers + test points"

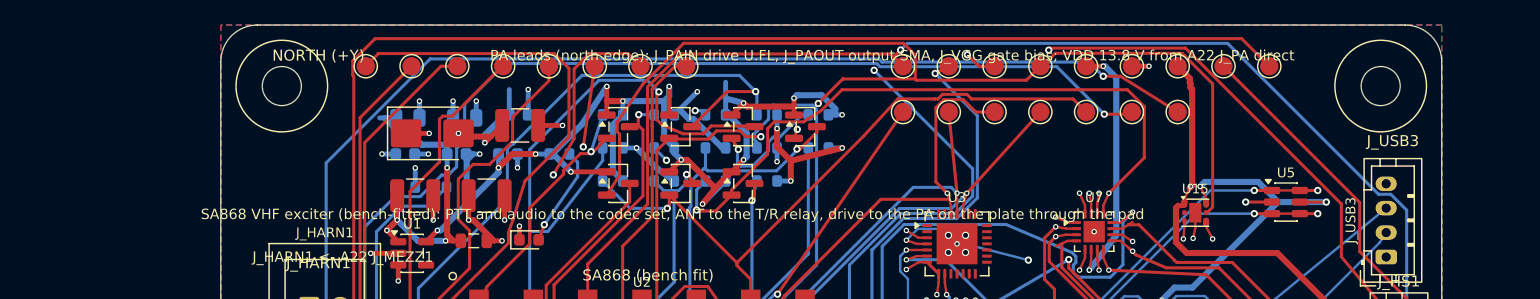
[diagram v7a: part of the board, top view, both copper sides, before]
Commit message: fix(ecad): D8 silk legend names the south edge for the PA leads (post-route text swap, deliverable rebuilt) [MESHSAT-830]
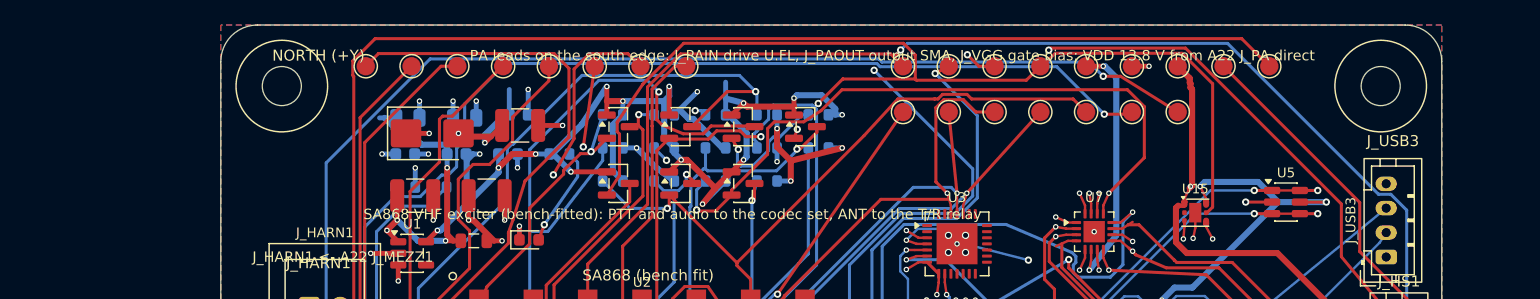
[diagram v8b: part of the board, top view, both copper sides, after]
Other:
- board text added: "PA leads on the south edge: J_PAIN drive U.FL, J_PAOUT output SMA, J_VGG gate bias; VDD 13.8 V from A22 J_PA direct"
- board text added: "SA868 VHF exciter (bench-fitted): PTT and audio to the codec set, ANT to the T/R relay"
- board text removed: "PA leads (north edge): J_PAIN drive U.FL, J_PAOUT output SMA, J_VGG gate bias; VDD 13.8 V from A22 J_PA direct"
- board text removed: "SA868 VHF exciter (bench-fitted): PTT and audio to the codec set, ANT to the T/R relay, drive to the PA on the plate through the pad"
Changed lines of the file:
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@@
 		)
 	)
-	(gr_text "SA868 VHF exciter (bench-fitted): PTT and audio to the codec set, ANT to the T/R relay, drive to the PA on the plate through the pad"
+	(gr_text "SA868 VHF exciter (bench-fitted): PTT and audio to the codec set, ANT to the T/R relay"
 		(at 87 75.5 0)
 		(layer "F.SilkS")
@@
 		)
 	)
-	(gr_text "PA leads (north edge): J_PAIN drive U.FL, J_PAOUT output SMA, J_VGG gate bias; VDD 13.8 V from A22 J_PA direct"
+	(gr_text "PA leads on the south edge: J_PAIN drive U.FL, J_PAOUT output SMA, J_VGG gate bias; VDD 13.8 V from A22 J_PA direct"
 		(at 105 62.5 0)
 		(layer "F.SilkS")
